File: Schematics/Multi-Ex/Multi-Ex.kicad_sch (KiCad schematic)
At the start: 1 part

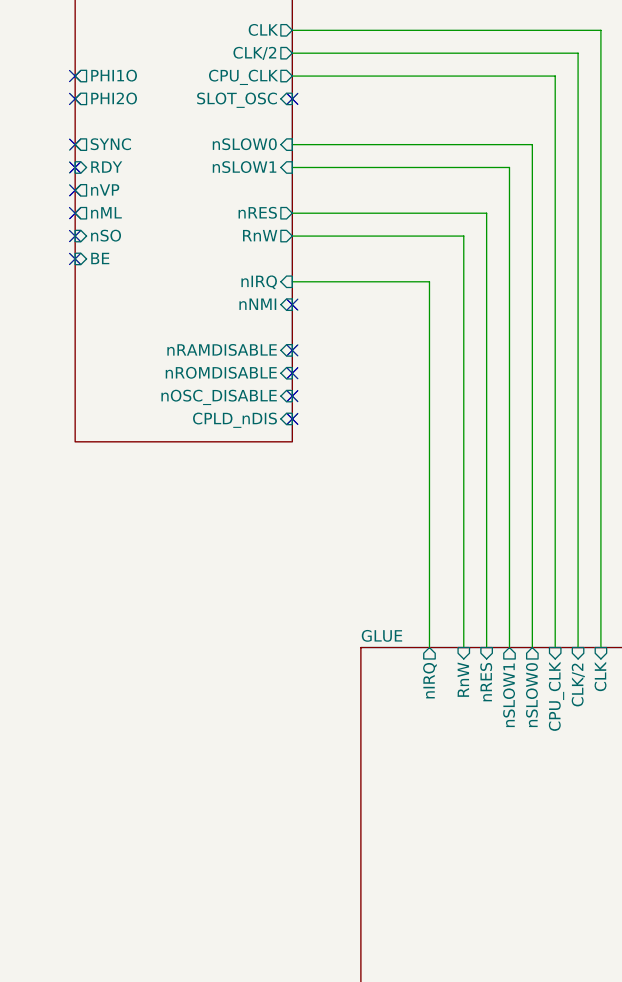
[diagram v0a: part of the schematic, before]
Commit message: Multi-expansion card routed.
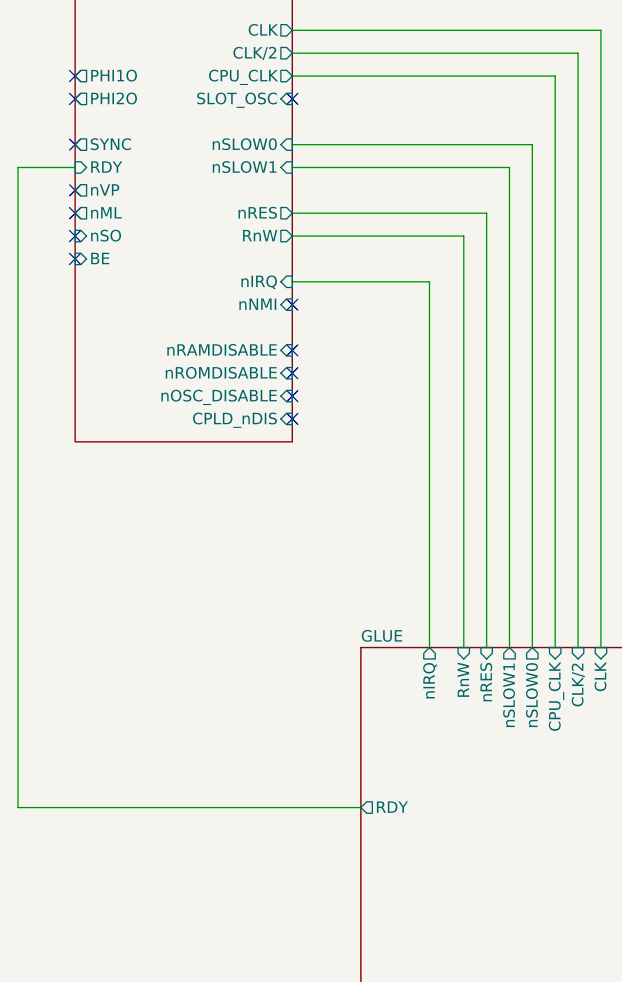
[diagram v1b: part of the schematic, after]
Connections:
- no-connect marks 14 -> 13
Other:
- sheet GLUE ports: added RDY; removed none
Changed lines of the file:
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@@
-	)
-	(no_connect
-		(at 31.75 58.42)
 	)
 	(no_connect
@@
 	(wire
 		(pts
+			(xy 63.5 129.54) (xy 25.4 129.54)
+		)
+		(stroke
+			(width 0)
+			(type default)
+		)
+	)
+	(wire
+		(pts
 			(xy 85.09 48.26) (xy 55.88 48.26)
 		)
@@
 	(wire
 		(pts
+			(xy 25.4 129.54) (xy 25.4 58.42)
+		)
+		(stroke
+			(width 0)
+			(type default)
+		)
+	)
+	(wire
+		(pts
 			(xy 156.21 76.2) (xy 156.21 111.76)
 		)
@@
 		(pts
 			(xy 55.88 55.88) (xy 82.55 55.88)
+		)
+		(stroke
+			(width 0)
+			(type default)
+		)
+	)
+	(wire
+		(pts
+			(xy 25.4 58.42) (xy 31.75 58.42)
 		)
 		(stroke
@@
 			)
 		)
+		(pin "RDY" output
+			(at 63.5 129.54 180)
+			(effects
+				(font
+					(size 1.27 1.27)
+				)
+				(justify left)
+			)
+		)
